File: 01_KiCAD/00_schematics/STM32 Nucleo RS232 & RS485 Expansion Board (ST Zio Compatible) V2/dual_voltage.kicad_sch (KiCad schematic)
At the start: 24 parts, among them U1 TLV77518PDBVR, U2 TPS2117DRLR

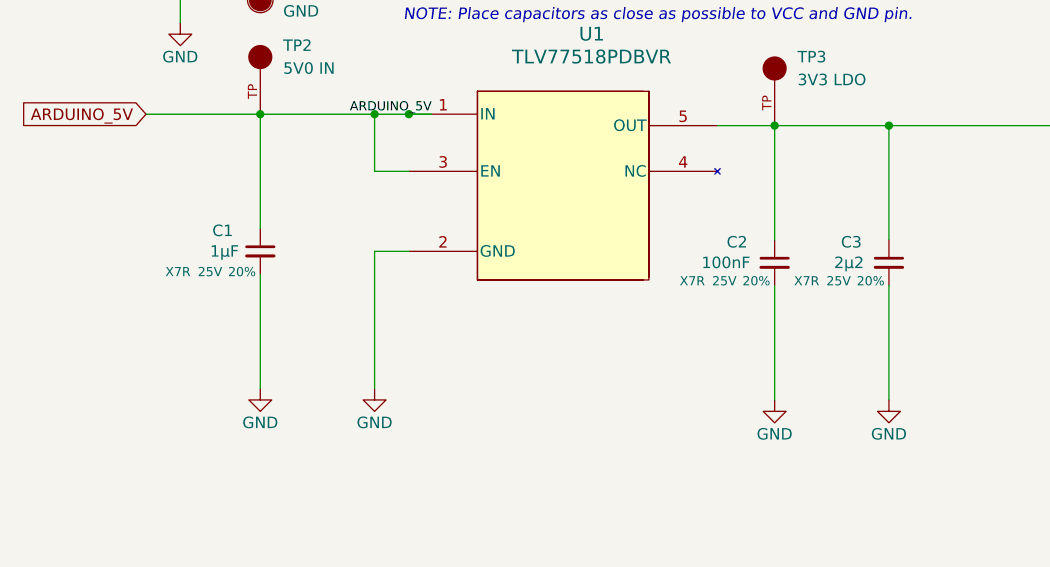
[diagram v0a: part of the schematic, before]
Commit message: Updated components
Updated components descriptions and partnumbers of C1, C2, C3, U1, TP1, TP2 and TP3
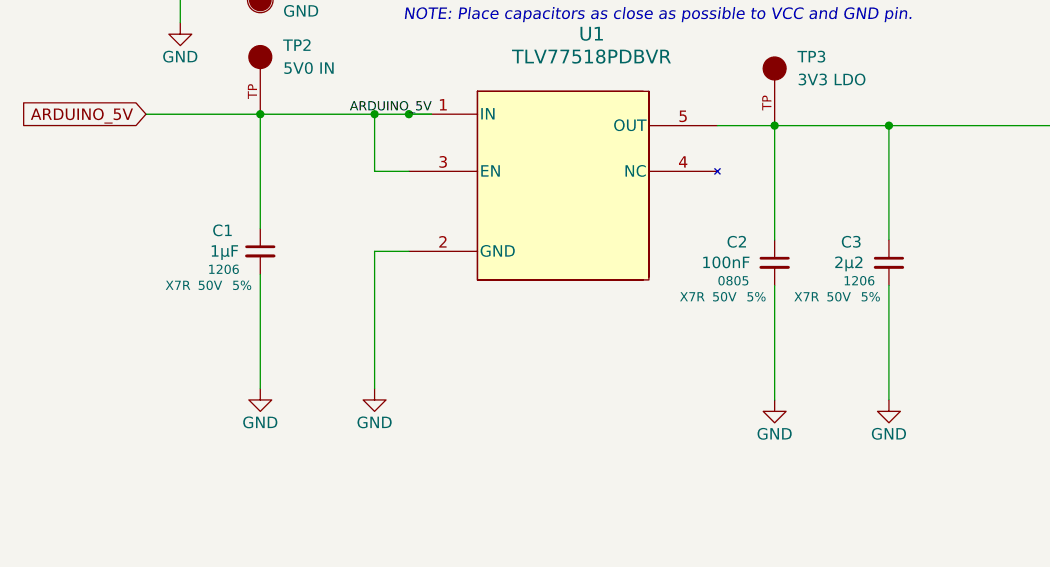
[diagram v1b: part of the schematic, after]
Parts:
- C1: LCSC C577426 -> C597503; MPN CS0805KKX7R9BB105 -> 12065C105JAT2A; Manufacturer YAGEO -> Kyocera AVX; Mouser PN (none) -> 581-12065C105JAT2A; PROD_ID CAP-00810 -> (none); Package 0805 -> 1206; Tolerance 20% -> 5%; Voltage 25V -> 50V; Voltage Rating 50V -> (none)
- C2: LCSC C125847 -> C2167095; MPN CC0805KKX7R9BB225 -> C0805C104J5RACTU; Manufacturer YAGEO -> KEMET; Mouser PN (none) -> 80-C0805C104J5R; PROD_ID CAP-00810 -> (none); Tolerance 20% -> 5%; Voltage 25V -> 50V; Voltage Rating 50V -> (none)
- C3: LCSC C125847 -> C1513220; MPN CC0805KKX7R9BB225 -> C1206C225J5RECAUTO; Manufacturer YAGEO -> KEMET; Mouser PN (none) -> 80-C1206C225J5RECAUT; Package 0805 -> 1206; Tolerance 20% -> 5%; Voltage 25V -> 50V; Voltage Rating 50V -> (none)
- TP2: LCSC (none) -> C2906763; MPN (none) -> 5005; Manufacturer (none) -> Keystone Electronics; Mouser PN (none) -> 534-5005; Type (none) -> THT
- TP3: LCSC (none) -> C2906763; MPN (none) -> 5005; Manufacturer (none) -> Keystone Electronics; Mouser PN (none) -> 534-5005; SNAPEDA_PN 5006 -> 5005; Type (none) -> THT
- U1: LCSC (none) -> C49292340; MPN (none) -> TLV77518PDBVR; Manufacturer (none) -> TI; Mouser PN (none) -> 595-TLV77518PDBVR; Package (none) -> SOT-23-5

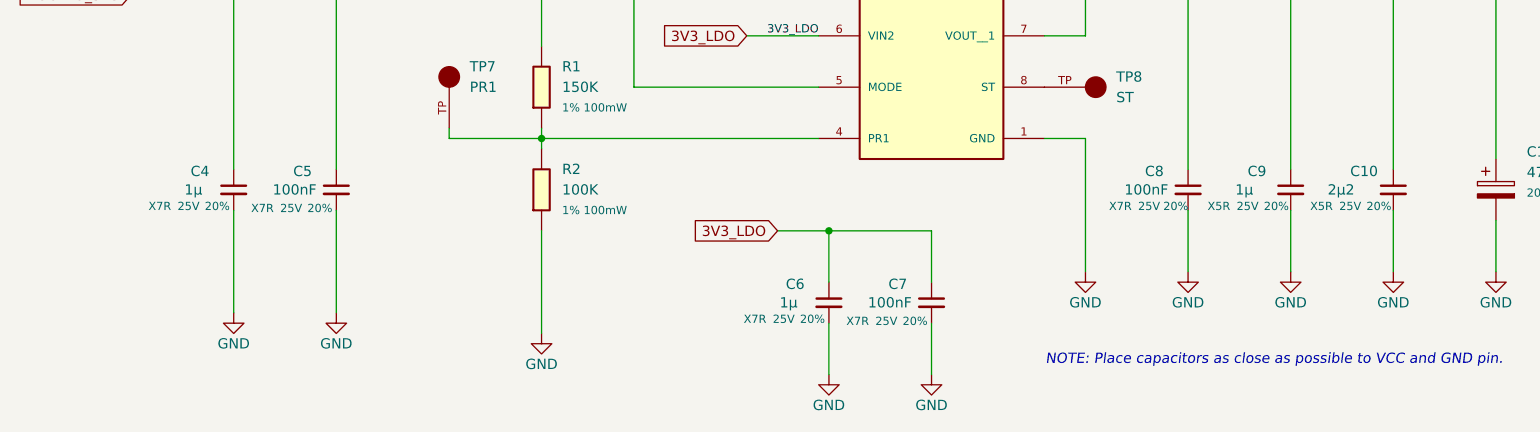
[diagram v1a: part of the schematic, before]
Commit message: Final revision checkup
After BOM-update and corrected some footprints and package sizes for resistors and capacitors, updated the PCB to "HW REV A0.2" as final PCB layout. Need to run DRC check before final approval.
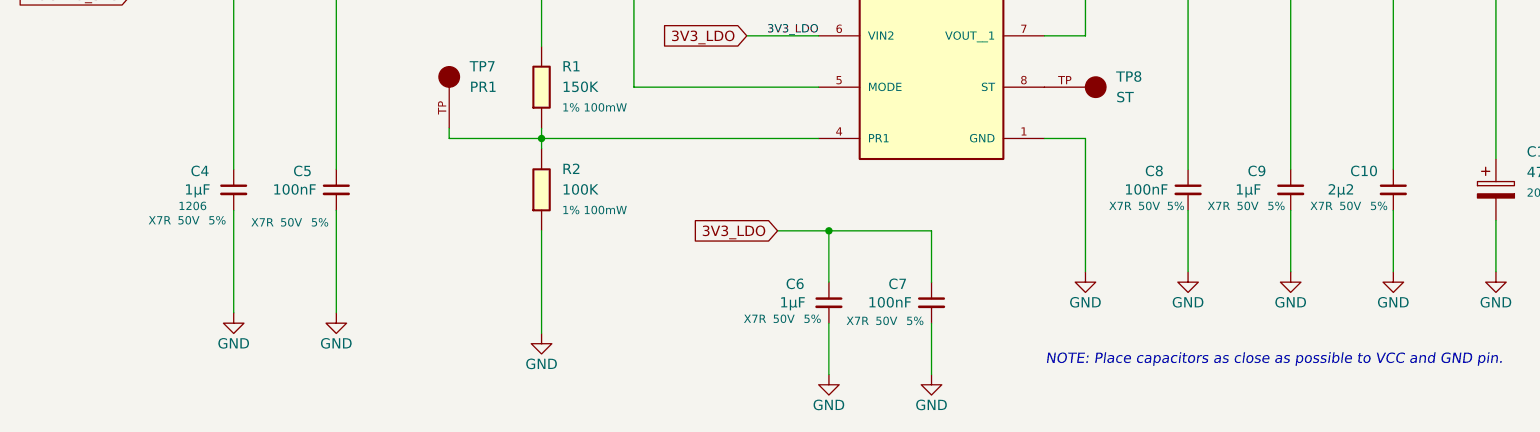
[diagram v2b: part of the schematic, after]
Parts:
- C10: Dielectric X5R -> X7R; LCSC C394395 -> C1513220; MPN EMK325ABJ107MM-T -> C1206C225J5RECAUTO; Manufacturer Taiyo Yuden -> KEMET; Mouser PN (none) -> 80-C1206C225J5RECAUT; PROD_ID CAP-00810 -> (none); Package 1210 -> 1206; Tolerance 20% -> 5%; Voltage 25V -> 50V; Voltage Rating 50V -> (none)
- C11, C12: Mouser PN (none) -> 667-EEE-FT1H470AP; Tolerance (none) -> 20%; Voltage (none) -> 50V
- C4, C6: value 1µ -> 1µF; LCSC C125847 -> C597503; MPN CC0805KKX7R9BB225 -> 12065C105JAT2A; Manufacturer YAGEO -> Kyocera AVX; Mouser PN (none) -> 581-12065C105JAT2A; PROD_ID CAP-00810 -> (none); Package 0805 -> 1206; Tolerance 20% -> 5%; Voltage 25V -> 50V; Voltage Rating 50V -> (none)
- C5: LCSC C577426 -> C2167095; MPN CS0805KKX7R9BB105 -> C0805C104J5RACTU; Manufacturer YAGEO -> KEMET; Mouser PN (none) -> 80-C0805C104J5R; PROD_ID CAP-00810 -> (none); Tolerance 20% -> 5%; Voltage 25V -> 50V; Voltage Rating 50V -> (none)
- C7: LCSC C577426 -> C2167095; MPN CS0805KKX7R9BB105 -> C0805C104J5RACTU; Manufacturer YAGEO -> KEMET; Mouser PN (none) -> 80-C0805C104J5R; Tolerance 20% -> 5%; Voltage 25V -> 50V
- C8: LCSC C24452 -> C2167095; MPN Samsung Electro-Mechanics -> C0805C104J5RACTU; Manufacturer Samsung Electro-Mechanics -> KEMET; Mouser PN (none) -> 80-C0805C104J5R; Package 0603 -> 0805; Tolerance 20% -> 5%; Voltage 25V -> 50V
- C9: value 1µ -> 1µF; Dielectric X5R -> X7R; LCSC C2932476 -> C597503; MPN CL21A106KBYQNNE -> 12065C105JAT2A; Manufacturer Samsung Electro-Mechanics -> Kyocera AVX; Mouser PN (none) -> 581-12065C105JAT2A; PROD_ID CAP-00810 -> (none); Package 0805 -> 1206; Tolerance 20% -> 5%; Voltage 25V -> 50V
- R1: LCSC C114660 -> C20142013; MPN RC0603FR-07150KL -> AC0603FR-7W150KL; Mouser PN (none) -> 603-AC0603FR-7W150KL
- R2: LCSC C14675 -> C5552302; MPN RC0603FR-07100KL -> AC0603FR-7W100KL; Mouser PN (none) -> 603-AC0603FR-7W100KL
- TP1, TP4: LCSC (none) -> C2906764; MPN (none) -> 5006; Manufacturer (none) -> Keystone Electronics; Mouser PN (none) -> 534-5006; Package NON STANDARD-1 Keystone -> Through Hole,P=2.54mm; Series (none) -> Compact-Series; Type (none) -> THT
- TP2, TP3: Package NON STANDARD-1 Keystone -> Through Hole,P=2.54mm; Series (none) -> Compact-Series
- TP5: LCSC (none) -> C2906763; MPN (none) -> 5005; Manufacturer (none) -> Keystone Electronics; Mouser PN (none) -> 534-5005; Package NON STANDARD-1 Keystone -> Through Hole,P=2.54mm; SNAPEDA_PN 5006 -> 5005; Series (none) -> Compact-Series; Type (none) -> THT
- TP6, TP7: LCSC (none) -> C2906763; MPN (none) -> 5005; Manufacturer (none) -> Keystone Electronics; Mouser PN (none) -> 534-5005; Package NON STANDARD-1 Keystone -> Through Hole,P=2.54mm; Series (none) -> Compact-Series; Type (none) -> THT
- TP8: LCSC (none) -> C2906763; MPN (none) -> 5005; Manufacturer (none) -> Keystone Electronics§; Mouser PN (none) -> 534-5005; Package NON STANDARD-1 Keystone -> Through Hole,P=2.54mm; Series (none) -> Compact-Series; Type (none) -> THT
- U1: Type (none) -> SMD
- U2: LCSC (none) -> C22399676; MPN (none) -> TPS2117DRLR; Manufacturer (none) -> TI; Mouser PN (none) -> 595-TPS2117DRLR; Package SOT-583 Texas Instruments -> SOT-5X3; Type (none) -> SMD

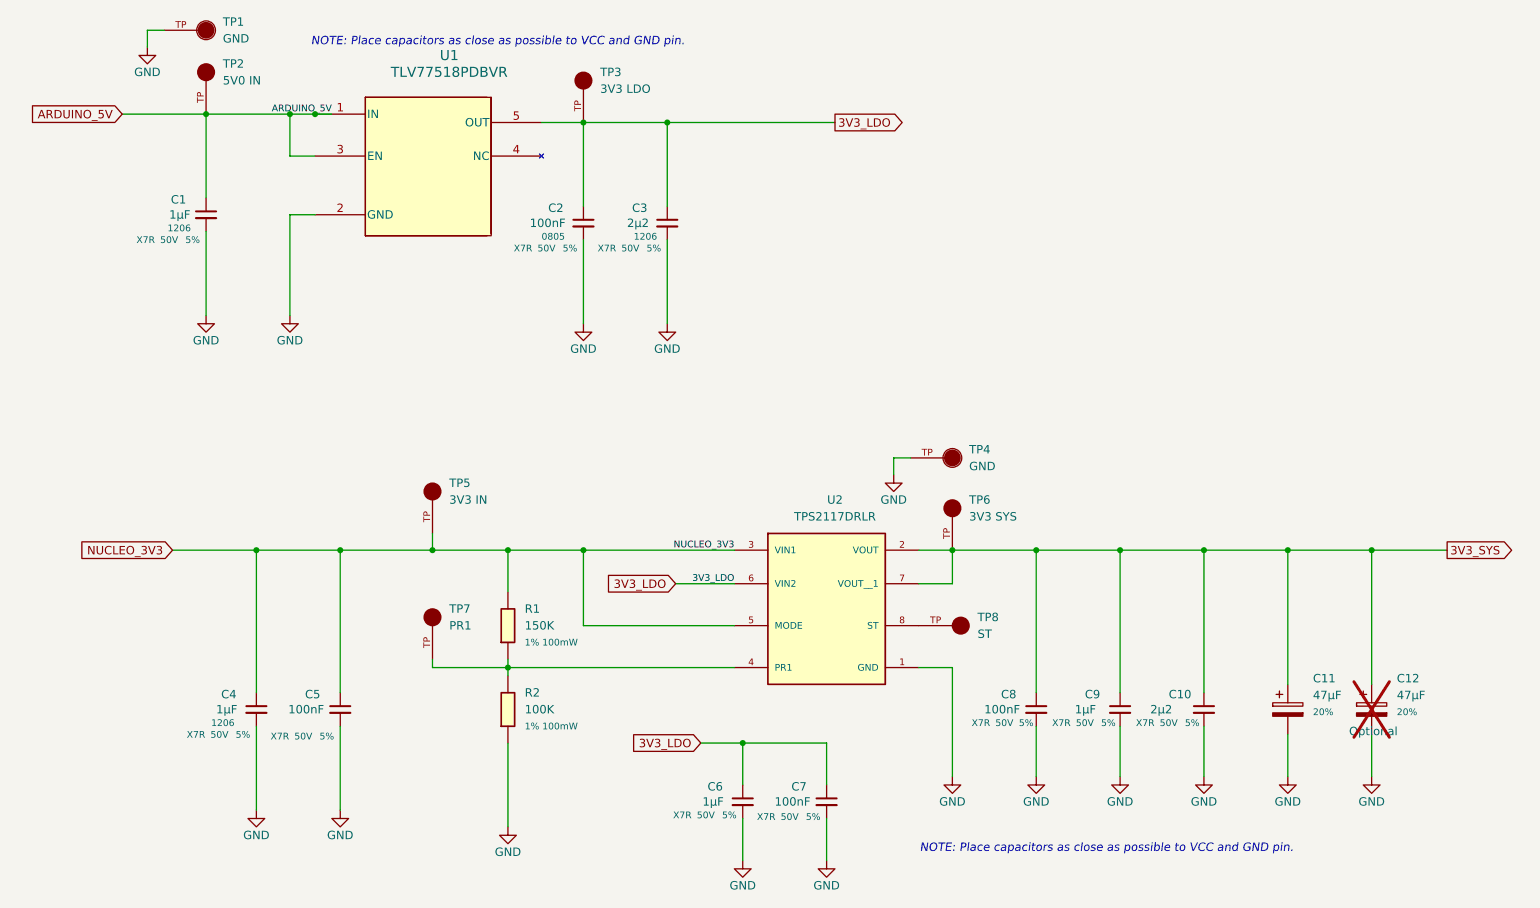
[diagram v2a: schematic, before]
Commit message: Changed to HR_REVA0.3
Updates design to PCB HW-REVA0.3 with the folowing changes:

CL_HW_2026_0001
Replaced text on silkscreen D3=>RX and D4=>TX.

CL_HW_2026_0002
Changed MCU_SHDN pin for THVD4431 from CN9-30 to CN9-11 to make it also Arduino compatible
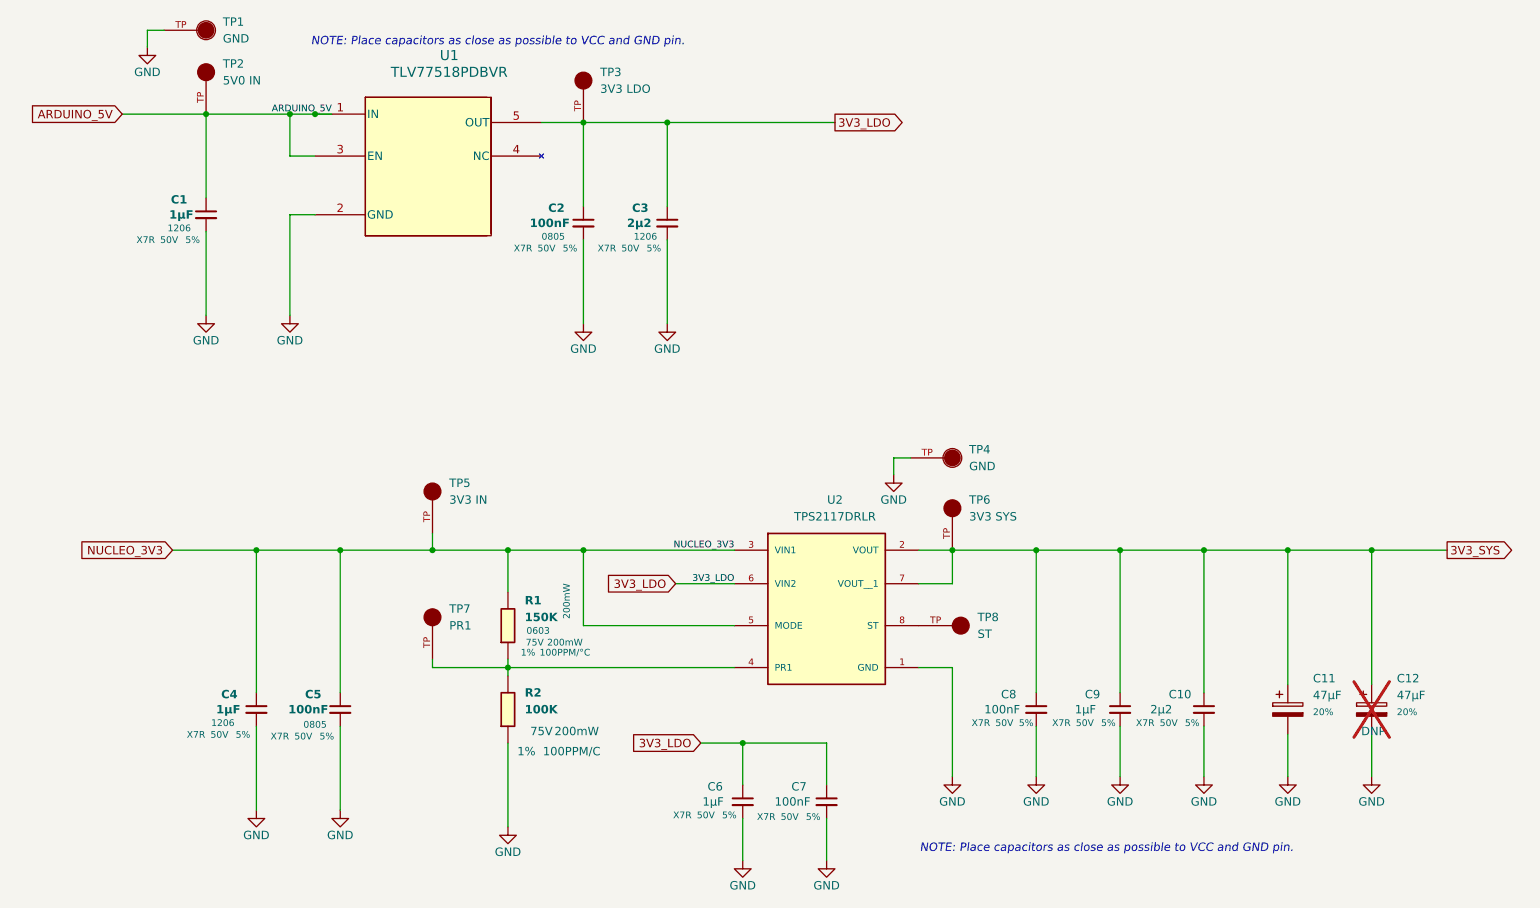
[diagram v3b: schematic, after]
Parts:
- C12: DNP Optional -> DNP
- R1: Power Ratin (none) -> 200mW; Power Rating (none) -> 200mW; Temperature Coefficient (none) -> 100PPM/°C; Tolerance (none) -> 1%; Voltage (none) -> 75V; Voltage Rating 1% 100mW -> (none)
- R2: Power Rating (none) -> 200mW; Temperature Coefficient (none) -> 100PPM/C; Tolerance (none) -> 1%; Voltage (none) -> 75V; Voltage Rating 1% 100mW -> (none)
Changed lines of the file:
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@@
 			)
 		)
-		(property "DNP" "Optional"
+		(property "DNP" "DNP"
 			(at 246.634 131.572 0)
 			(effects
@@
 			)
 		)
+		(property "Farnell PN" ""
+			(at 246.38 128.27 0)
+			(effects
+				(font
+					(size 1.27 1.27)
+				)
+				(hide yes)
+			)
+		)
+		(property "DigiKey PN" ""
+			(at 246.38 128.27 0)
+			(effects
+				(font
+					(size 1.27 1.27)
+				)
+				(hide yes)
+			)
+		)
+		(property "Series" ""
+			(at 246.38 128.27 0)
+			(effects
+				(font
+					(size 1.27 1.27)
+				)
+				(hide yes)
+			)
+		)
 		(pin "1"
 		)
@@
 				(font
 					(size 1.27 1.27)
+					(thickness 0.254)
+					(bold yes)
 				)
 				(justify left)
@@
 				(font
 					(size 1.27 1.27)
+					(thickness 0.254)
+					(bold yes)
 					(color 72 0 72 1)
 				)
@@
 		)
 		(property "Package" "0805"
-			(at 90.17 128.27 0)
+			(at 86.36 130.556 0)
 			(effects
 				(font
-					(size 1.27 1.27)
+					(size 1.016 1.016)
+					(color 194 0 194 1)
 				)
-				(hide yes)
 			)
 		)
@@
 		(on_board yes)
 		(dnp no)
-		(fields_autoplaced yes)
 		(property "Reference" "R2"
-			(at 118.11 125.7299 0)
+			(at 118.11 125.73 0)
 			(effects
 				(font
 					(size 1.27 1.27)
+					(thickness 0.254)
+					(bold yes)
 				)
 				(justify left)
@@
 		)
 		(property "Value" "100K"
-			(at 118.11 128.2699 0)
+			(at 118.11 128.27 0)
 			(effects
 				(font
 					(size 1.27 1.27)
+					(thickness 0.254)
+					(bold yes)
+					(color 72 0 72 1)
 				)
 				(justify left)
@@
 					(size 1.27 1.27)
 				)
+				(hide yes)
 			)
 		)
-		(property "Voltage Rating" "1% 100mW"
+		(property "Voltage Rating" ""
 			(at 118.11 130.8099 0)
 			(effects
@@
 				)
 				(justify left)
+				(hide yes)
 			)
 		)
@@
 			)
 		)
+		(property "Farnell PN" ""
+			(at 115.57 128.27 0)
+			(effects
+				(font
+					(size 1.27 1.27)
+				)
+				(hide yes)
+			)
+		)
+		(property "DigiKey PN" ""
+			(at 115.57 128.27 0)
+			(effects
+				(font
+					(size 1.27 1.27)
+				)
+				(hide yes)
+			)
+		)
+		(property "Series" ""
+			(at 115.57 128.27 0)
+			(effects
+				(font
+					(size 1.27 1.27)
+				)
+				(hide yes)
+			)
+		)
+		(property "Voltage" "75V"
+			(at 120.65 131.572 0)
+			(effects
+				(font
+					(size 1.27 1.27)
+				)
+			)
+		)
+		(property "Tolerance" "1%"
+			(at 118.364 134.62 0)
+			(effects
+				(font
+					(size 1.27 1.27)
+				)
+			)
+		)
+		(property "Power Rating" "200mW"
+			(at 125.984 131.572 0)
+			(effects
+				(font
+					(size 1.27 1.27)
+				)
+			)
+		)
+		(property "Temperature Coefficient" "100PPM/C"
+			(at 125.222 134.62 0)
+			(effects
+				(font
+					(size 1.27 1.27)
+				)
+			)
+		)
 		(pin "2"
 		)
@@
 				(font
 					(size 1.27 1.27)
+					(thickness 0.254)
+					(bold yes)
 				)
 				(justify left)
@@
 				(font
 					(size 1.27 1.27)
+					(thickness 0.254)
+					(bold yes)
 					(color 72 0 72 1)
 				)
@@
 				(font
 					(size 1.27 1.27)
+					(thickness 0.254)
+					(bold yes)
 				)
 				(justify left)
@@
 				(font
 					(size 1.27 1.27)
+					(thickness 0.254)
+					(bold yes)
 					(color 72 0 72 1)
 				)
@@
 				(font
 					(size 1.27 1.27)
+					(thickness 0.254)
+					(bold yes)
 				)
 				(justify left)
@@
 				(font
 					(size 1.27 1.27)
+					(thickness 0.254)
+					(bold yes)
 					(color 72 0 72 1)
 				)
@@
 				(font
 					(size 1.27 1.27)
+					(thickness 0.254)
+					(bold yes)
 				)
 				(justify left)
@@
 				(font
 					(size 1.27 1.27)
+					(thickness 0.254)
+					(bold yes)
 					(color 72 0 72 1)
 				)
@@
 	)
 	(symbol
+		(lib_name "R_0603_1")
 		(lib_id "PCM_fab:R_0603")
 		(at 115.57 115.57 0)
@@
 		(on_board yes)
 		(dnp no)
-		(fields_autoplaced yes)
 		(property "Reference" "R1"
-			(at 118.11 113.0299 0)
+			(at 118.11 111.76 0)
 			(effects
 				(font
 					(size 1.27 1.27)
+					(thickness 0.254)
+					(bold yes)
 				)
 				(justify left)
@@
 		)
 		(property "Value" "150K"
-			(at 118.11 115.5699 0)
+			(at 118.11 114.3 0)
 			(effects
 				(font
 					(size 1.27 1.27)
+					(thickness 0.254)
+					(bold yes)
+					(color 72 0 72 1)
 				)
 				(justify left)
@@
 			)
 		)
-		(property "Datasheet" "https://www.lcsc.com/datasheet/C20142013.pdf"
+		(property "Datasheet" "https://nl.mouser.com/datasheet/3/508/1/PYu-AC_51_RoHS_L_11.pdf"
 			(at 115.57 115.57 0)
 			(effects
@@
 			)
 		)
-		(property "Description" "200mW 150kΩ Thick Film Resistor ±100ppm/℃ ±1% 0603 Chip Resistor - Surface Mount RoHS"
+		(property "Description" "Resistor"
 			(at 115.57 115.57 0)
 			(effects
@@
 		)
 		(property "Package" "0603"
-			(at 115.57 115.57 0)
+			(at 120.142 116.332 0)
 			(effects
 				(font
-					(size 1.27 1.27)
+					(size 1.016 1.016)
+					(color 194 0 194 1)
 				)
-				(hide yes)
 			)
 		)
@@
 			)
 		)
-		(property "Voltage Rating" "1% 100mW"
+		(property "Voltage Rating" ""
 			(at 118.11 118.1099 0)
 			(effects
@@
 			)
 		)
+		(property "Farnell PN" ""
+			(at 115.57 115.57 0)
+			(effects
+				(font
+					(size 1.27 1.27)
+				)
+				(hide yes)
+			)
+		)
+		(property "DigiKey PN" ""
+			(at 115.57 115.57 0)
+			(effects
+				(font
+					(size 1.27 1.27)
+				)
+				(hide yes)
+			)
+		)
+		(property "Series" ""
+			(at 115.57 115.57 0)
+			(effects
+				(font
+					(size 1.27 1.27)
+				)
+				(hide yes)
+			)
+		)
+		(property "Voltage" "75V"
+			(at 119.634 118.11 0)
+			(effects
+				(font
+					(size 1.016 1.016)
+					(color 194 0 0 1)
+				)
+			)
+		)
+		(property "Tolerance" "1%"
+			(at 118.618 119.634 0)
+			(effects
+				(font
+					(size 1.016 1.016)
+					(color 194 0 0 1)
+				)
+			)
+		)
+		(property "Power Rating" "200mW"
+			(at 124.206 118.11 0)
+			(effects
+				(font
+					(size 1.016 1.016)
+					(color 194 0 0 1)
+				)
+			)
+		)
+		(property "Temperature Coefficient" "100PPM/°C"
+			(at 124.206 119.634 0)
+			(effects
+				(font
+					(size 1.016 1.016)
+					(color 194 0 0 1)
+				)
+			)
+		)
+		(property "Power Ratin" "200mW"
+			(at 124.46 114.554 90)
+			(effects
+				(font
+					(size 1.016 1.016)
+					(color 194 0 0 1)
+				)
+				(justify left)
+			)
+		)
